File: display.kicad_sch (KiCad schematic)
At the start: 17 parts, among them Q1 ZXM61N03F, U1 E2206KS0E1

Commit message: .
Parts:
- added A1: Arduino_Nano_Every, Module:Arduino_Nano, symbol rsx_Modules:Arduino_Nano_Every
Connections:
- net GND: now also A1.29 (GND), A1.4 (GND)
- net Connect to power switch: now reaches C10.1, C9.1, SRP3012TA-100M1.1, U1.15, U1.16
- net A2: now reaches U1.10
- net A3: now reaches U1.11
- net D2: now reaches U1.12
- net SCL: now reaches U1.13
- net SDA: now reaches U1.14
- net A0: now reaches U1.8
- net A1: now reaches U1.9
- new net 10: A1.21 (A2)
- new net 11: A1.22 (A3)
- new net 12: A1.5 (D2)
- new net 13: A1.24 (SCL/A5)
- new net 14: A1.23 (SDA/A4)
- new net 8: A1.19 (A0)
- new net 9: A1.20 (A1)

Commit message: Nano every
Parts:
- removed Q1: ZXM61N03F, Package_TO_SOT_SMD:SOT-23, symbol Transistor_FET:ZXM61N03F
- removed U1: E2206KS0E1, SOIC_096NL_PUL, symbol rsx_misc:Graphic Display
- added J3: FH34SRJ-24S-0.5SH_99_, rsx_headers_communications:HRS_FH34SRJ-24S-0.5SH_99_, symbol rsx_Header_communication:FH34SRJ-24S-0.5SH_99_
- added Q1, Q2: ZXM61N03F, rsx_packages_TO_SOT:SOT-23, symbol rsx_Transistors:ZXM61N03F
- added SW3: Button-THT - 2-1825910-7, rsx_HID:2-1825910-7, symbol rsx_HID:Button-THT - 2-1825910-7
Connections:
- net 12: now also A1.15 (MISO)
- net A0: now also J3.8
- net A1: now also J3.9
- net A2: now also J3.10
- net A3: now also J3.11
- net GND: now also J3.17
- net SCL: now also J3.13
- net SDA: now also J3.14
- net at C2.2: now also J3.18
- net at C6.2, CR3.1: now also J3.21
- net at R1.2: now also J3.3, Q1.2 (S)
- net at C7.2, CR1.2: now also J3.23
- net at C3.2: now also J3.20
- net at C4.2: now also J3.22
- net at C5.2: now also J3.24
- net at C1.2: now also J3.5
- net at A1.10 (D7): now also Q2.1 (G)
- net Display Power: now reaches A1.17 (3V3)
- net Display Power: now also Q2.3 (D)
- net at A1.30 (VIN): now also SW3.1
- net at C8.1, CR3.2, SRP3012TA-100M1.2: now also Q1.3 (D)
- net Connect to power switch: no longer names the net of C10.1, C9.1, SRP3012TA-100M1.1
- net Connect to power switch: now also J3.15, J3.16, Q2.2 (S)
- new net: J3.2, Q1.1 (G)
- new net +3.3V: SW3.2
- new net MISO: J3.12
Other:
- moved on the sheet: A1, C1, R1

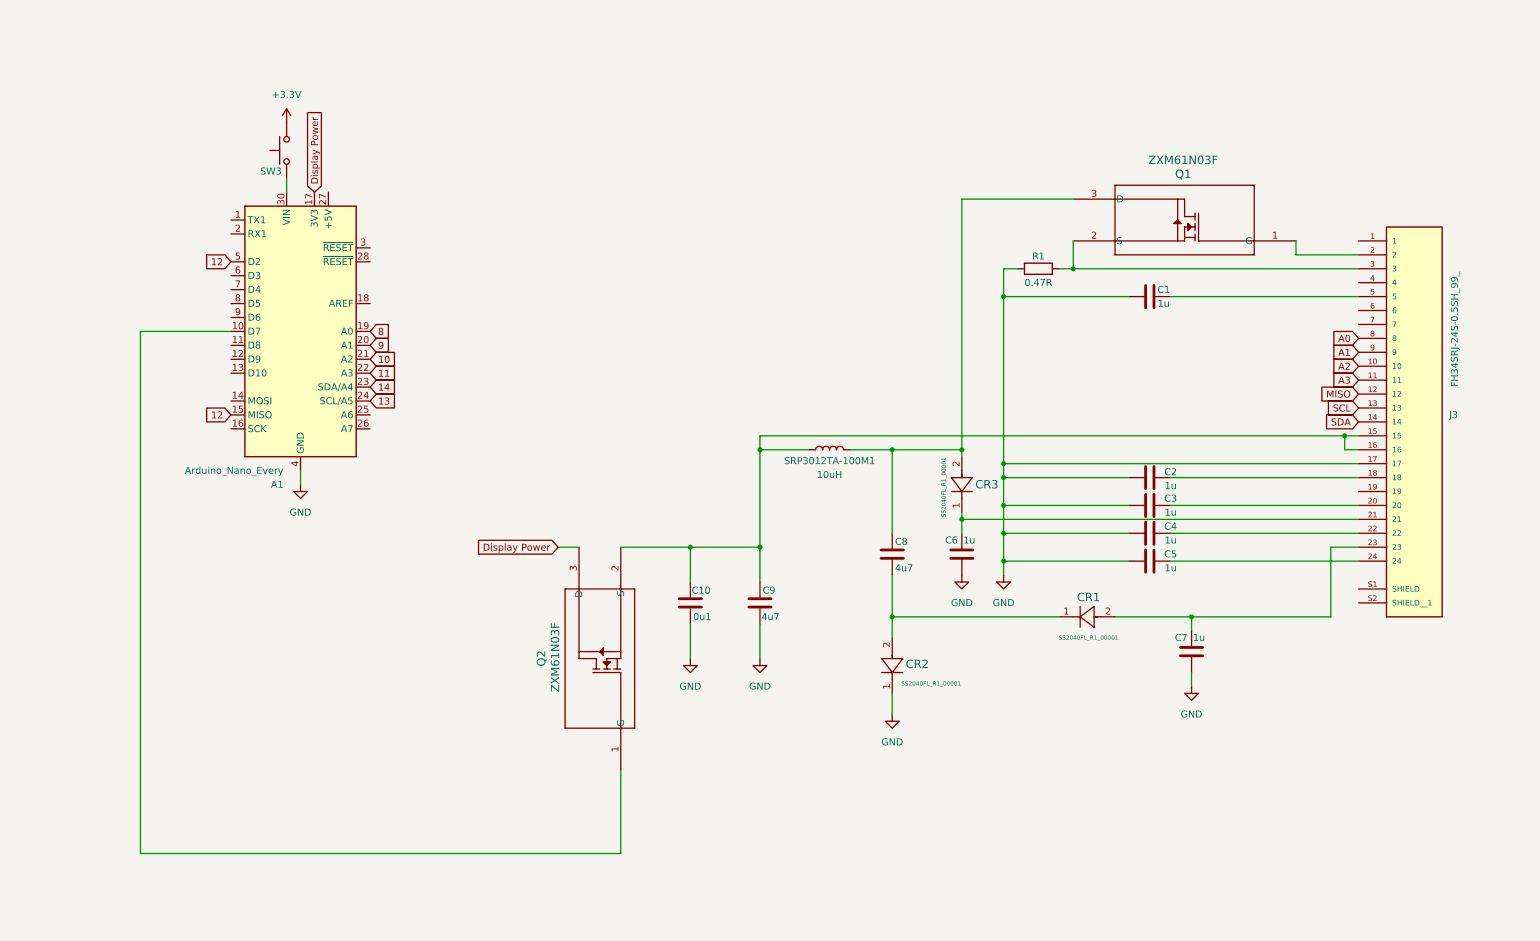
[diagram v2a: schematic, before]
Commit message: Schematic with Pico
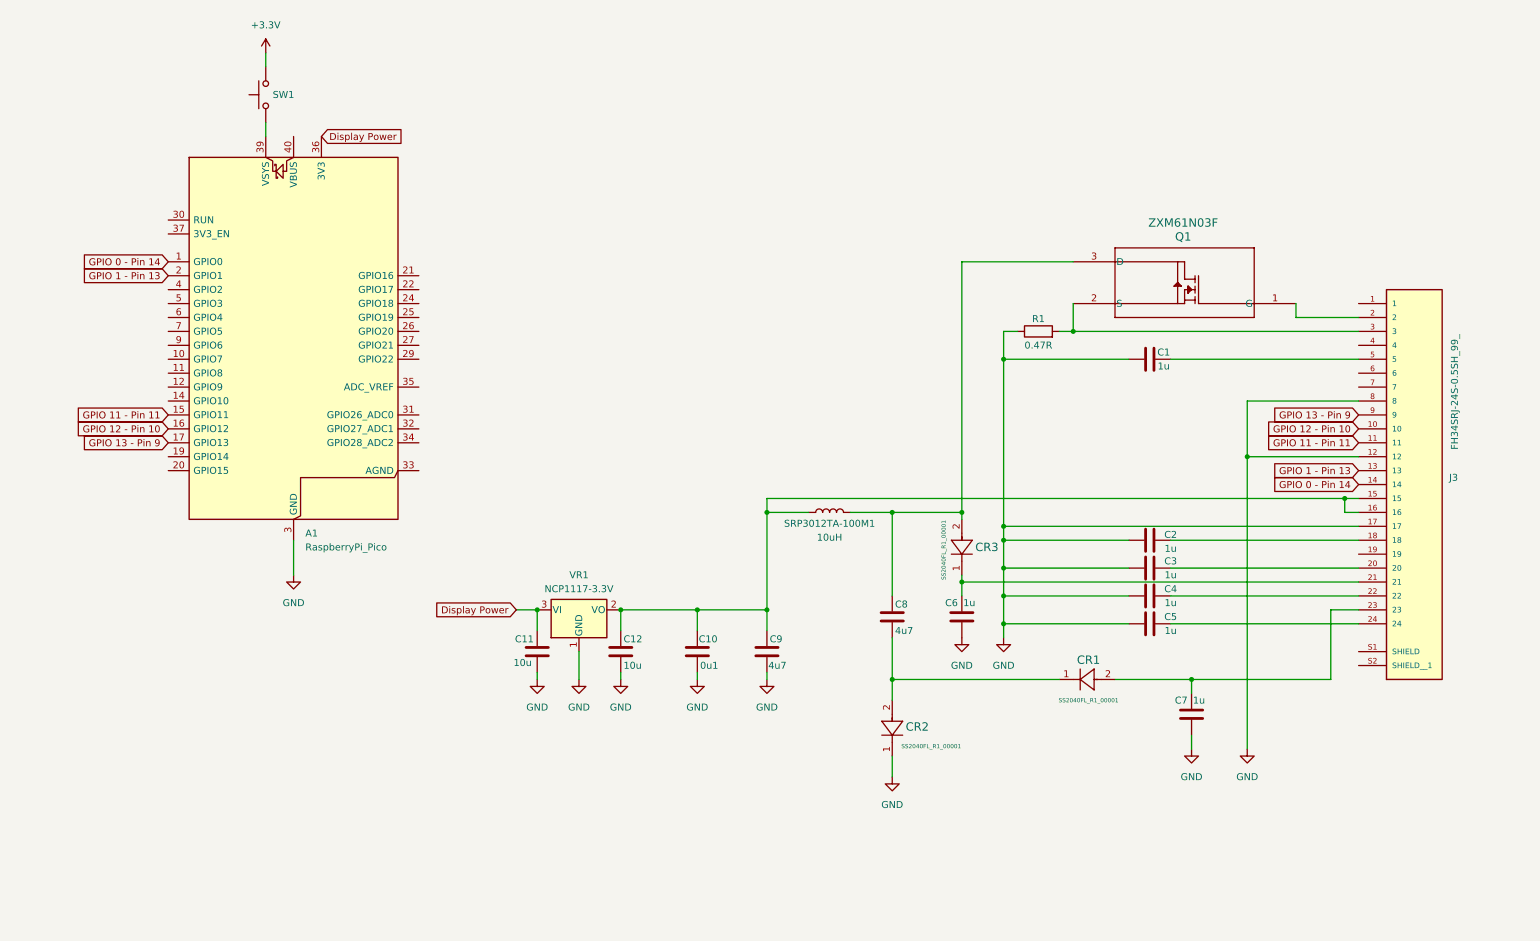
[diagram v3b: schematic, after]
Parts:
- removed A1: Arduino_Nano_Every, Module:Arduino_Nano, symbol rsx_Modules:Arduino_Nano_Every
- removed Q2: ZXM61N03F, rsx_packages_TO_SOT:SOT-23, symbol rsx_Transistors:ZXM61N03F
- removed SW3: Button-THT - 2-1825910-7, rsx_HID:2-1825910-7, symbol rsx_HID:Button-THT - 2-1825910-7
- added A1: RaspberryPi_Pico, Module:RaspberryPi_Pico_Common_Unspecified, symbol MCU_Module:RaspberryPi_Pico
- added C11, C12: 10u, rsx_capacitors:C_0805_2012Metric, symbol rsx_Capacitors:10u
- added SW1: Button-THT - 2-1825910-7, rsx_HID:2-1825910-7, symbol rsx_HID:Button-THT - 2-1825910-7
- added VR1: NCP1117-3.3V, rsx_packages_TO_SOT:SOT-223-3_TabPin2, symbol rsx_voltage_regulation:NCP1117-3.3V
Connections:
- net A0 is gone; now on net GND: J3.8
- net MISO is gone; now on net GND: J3.12
- net +3.3V: now also SW1.2
- net Display Power: now also A1.36 (3V3), C11.1, VR1.3 (VI)
- net GND: now also A1.13 (GND), A1.18 (GND), A1.23 (GND), A1.28 (GND), A1.3 (GND), A1.38 (GND), A1.8 (GND), C11.2, C12.2, VR1.1 (GND)
- net at C10.1, C9.1, J3.15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: now also C12.1, VR1.2 (VO)
- net A1 renamed GPIO 13 - Pin 9
- net GPIO 13 - Pin 9: now also A1.17 (GPIO13)
- net A2 renamed GPIO 12 - Pin 10
- net GPIO 12 - Pin 10: now also A1.16 (GPIO12)
- net A3 renamed GPIO 11 - Pin 11
- net GPIO 11 - Pin 11: now also A1.15 (GPIO11)
- net SCL renamed GPIO 1 - Pin 13
- net GPIO 1 - Pin 13: now also A1.2 (GPIO1)
- net SDA renamed GPIO 0 - Pin 14
- net GPIO 0 - Pin 14: now also A1.1 (GPIO0)
- new net: A1.39 (VSYS), SW1.1
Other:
- moved on the sheet: C1, C10, C2, C3, C4, C5, C6, C7, C8, C9, CR1, CR2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

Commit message: Pico connected to display (mostly???)
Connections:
- net +3.3V: now also SW1.1; no longer SW1.2
- net GND: no longer J3.12
- net at A1.39 (VSYS): now also SW1.2; no longer SW1.1
- net GP17 - Pin 12 CSB: now reaches A1.22 (GPIO17)
- net GP17 - Pin 12 CSB: now also J3.12
- net GP18 - Pin 13 SCL: now reaches A1.24 (GPIO18)
- net GP18 - Pin 13 SCL: now also J3.13
- net GP19 - Pin 14 SDA: now reaches A1.25 (GPIO19)
- net GP19 - Pin 14 SDA: now also J3.14
- net GPIO 0 - Pin 14: no longer names the net of A1.1 (GPIO0)
- net GPIO 0 - Pin 14: no longer J3.14
- net GPIO 1 - Pin 13: no longer names the net of A1.2 (GPIO1)
- net GPIO 1 - Pin 13: no longer J3.13
- net GPIO 11 - Pin 11 renamed GP11 - Pin 10 RST
- net GP11 - Pin 10 RST: no longer J3.11
- net GPIO 12 - Pin 10 renamed GP12 - Pin 10
- net GP12 - Pin 10: no longer A1.16 (GPIO12)
- net GPIO 13 - Pin 9 renamed GP13 - Pin 9
- net GP13 - Pin 9: no longer A1.17 (GPIO13)
- new net GP11 - Pin 11: J3.11
- new net GP12 - Pin 11 DC: A1.16 (GPIO12)
- new net GP13 - Pin 9 Busy: A1.17 (GPIO13)
- no-connect marks 0 -> 32
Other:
- moved on the sheet: A1, CR2, SW1

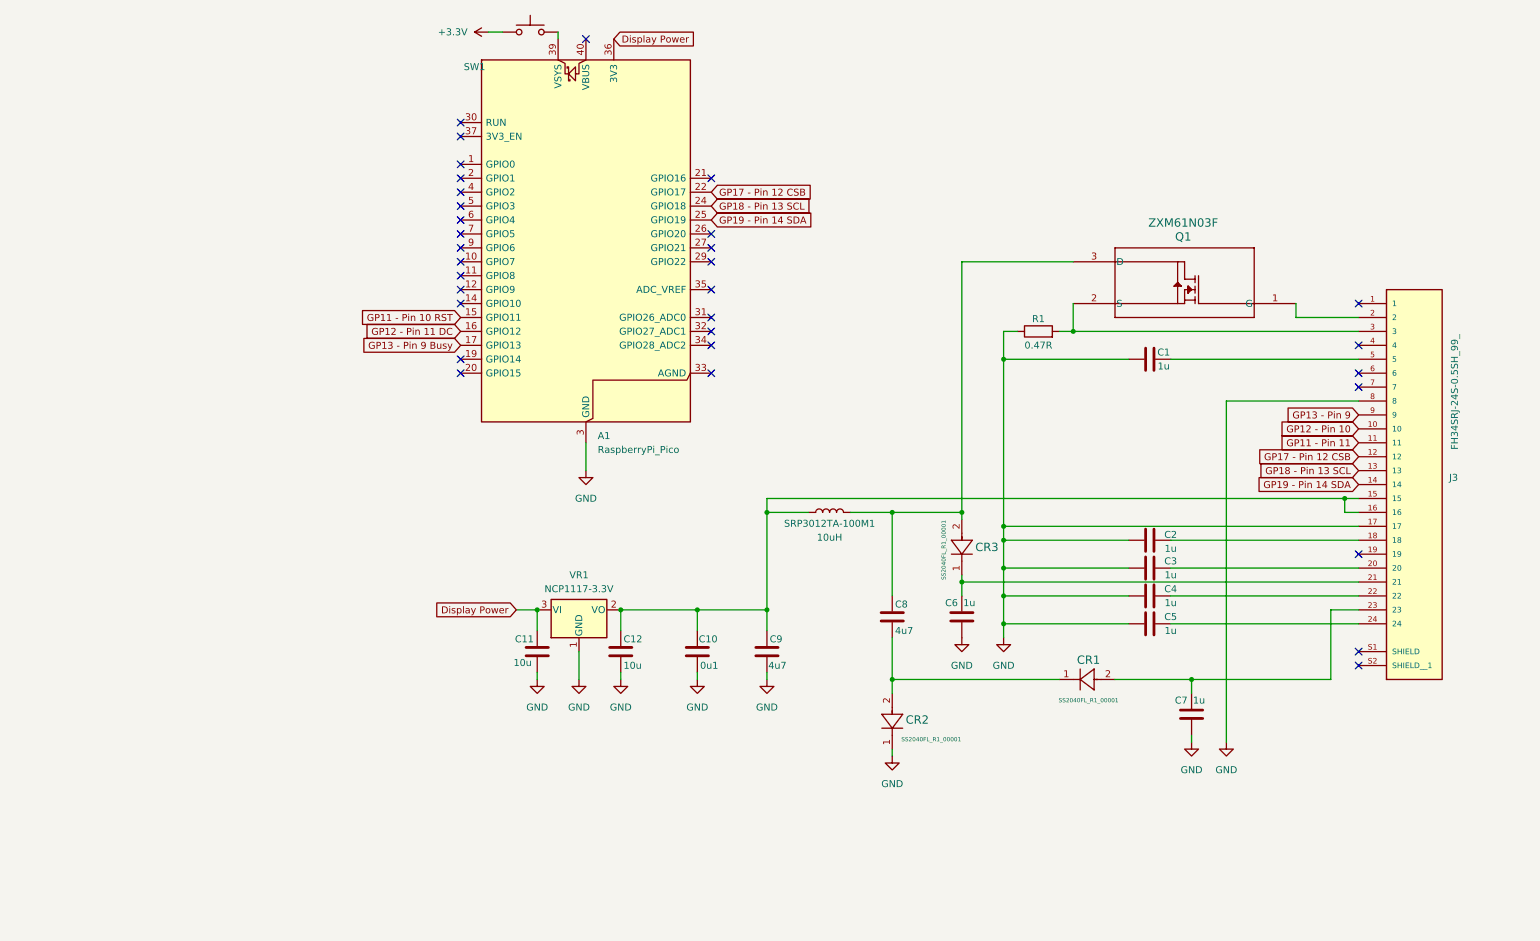
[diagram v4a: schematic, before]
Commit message: Display + Pico + voltage regulator
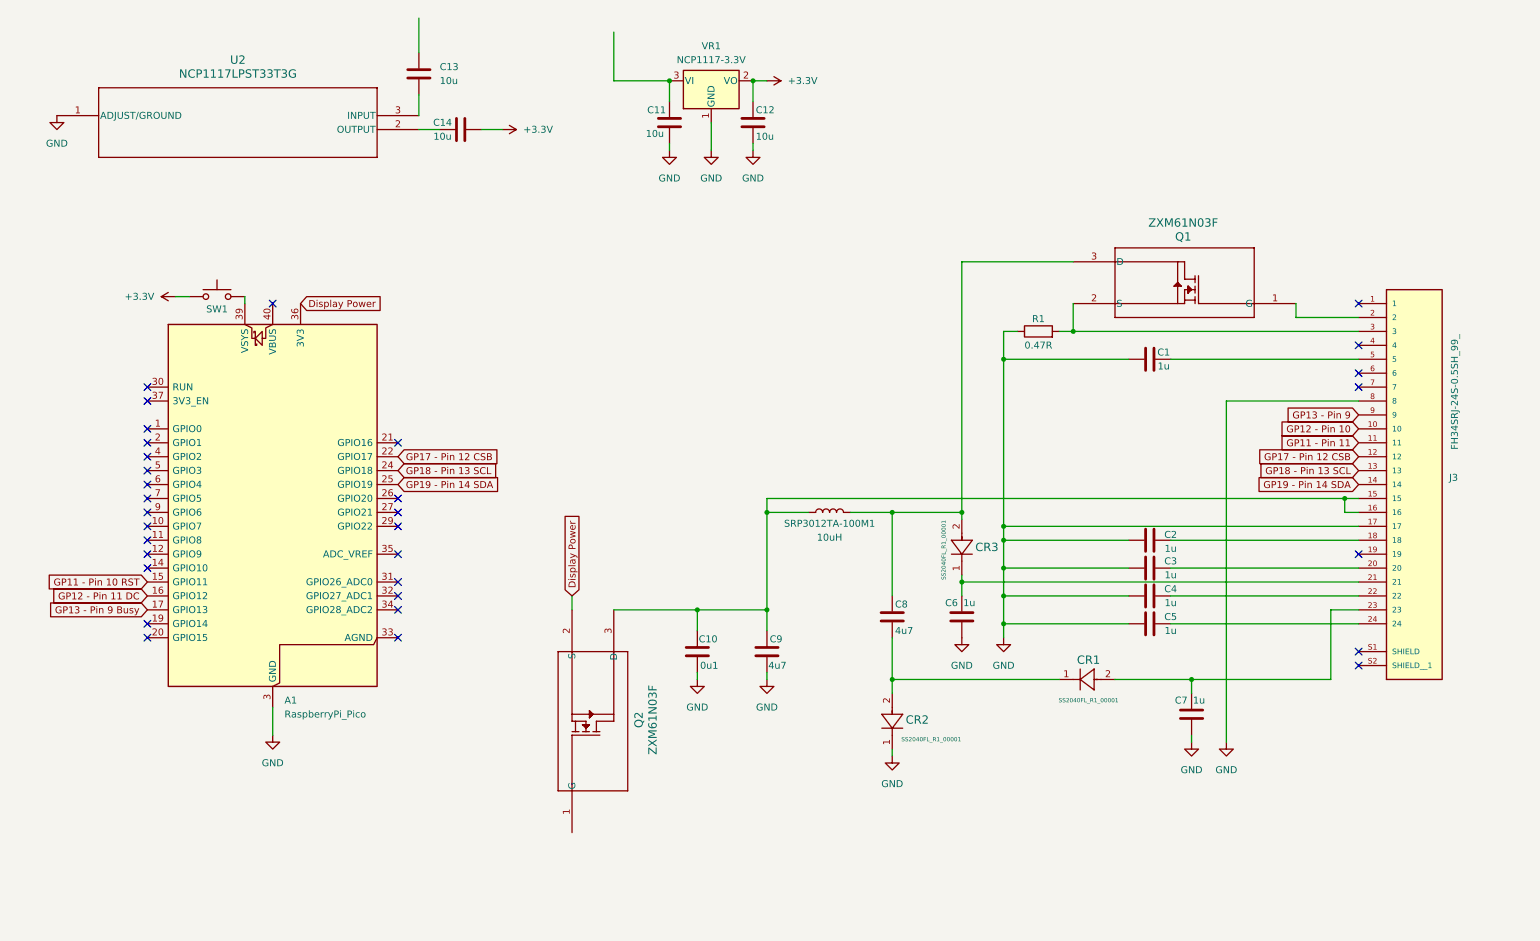
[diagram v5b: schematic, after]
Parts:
- added C13, C14: 10u, rsx_capacitors:C_0805_2012Metric, symbol rsx_Capacitors:10u
- added Q2: ZXM61N03F, rsx_packages_TO_SOT:SOT-23, symbol rsx_Transistors:ZXM61N03F
- added U2: NCP1117LPST33T3G, SOT223-3_ONS, symbol NCP1117:NCP1117LPST33T3G
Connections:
- net +3.3V: now also C12.1, VR1.2 (VO), C14.2
- net Display Power: now also Q2.2 (S); no longer C11.1, VR1.3 (VI)
- net GND: now also U2.1 (ADJUST/GROUND)
- net at C10.1, C9.1, J3.15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: now also Q2.3 (D); no longer C12.1, VR1.2 (VO)
- new net: C14.1, U2.2 (OUTPUT)
- new net: C13.2, U2.3 (INPUT)
- new net: C11.1, VR1.3 (VI)
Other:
- moved on the sheet: A1, C11, C12, SW1, VR1

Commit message: new
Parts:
- added C15: C, symbol Device:C
- added R2: R, symbol Device:R
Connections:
- net GND: now also C15.2
- net at SW1.2: now also A1.40 (VBUS); no longer A1.39 (VSYS)
- net at C10.1, C9.1, J3.15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: now also Q2.2 (S); no longer Q2.3 (D)
- net at Q2.1 (G): now also C15.1, R2.2
- net Display Power: no longer names the net of A1.36 (3V3)
- net Display Power: no longer Q2.2 (S)
- new net display power: Q2.3 (D)
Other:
- moved on the sheet: CR2, SW1

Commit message: Update display.kicad_sch
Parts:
- removed C12, C13, C14: 10u, rsx_capacitors:C_0805_2012Metric, symbol rsx_Capacitors:10u
- removed C15: C, symbol Device:C
- removed R2: R, symbol Device:R
- removed U2: NCP1117LPST33T3G, SOT223-3_ONS, symbol NCP1117:NCP1117LPST33T3G
- removed VR1: NCP1117-3.3V, rsx_packages_TO_SOT:SOT-223-3_TabPin2, symbol rsx_voltage_regulation:NCP1117-3.3V
- added C16, C18: 10u, rsx_capacitors:C_0805_2012Metric, symbol rsx_Capacitors:10u
- added R2: 100K, rsx_resistors:R_0603_1608Metric, symbol rsx_Resistors:100K
- added R4: 330R, rsx_resistors:R_0603_1608Metric, symbol rsx_Resistors:330R
- added U1: NCP1117LPST33T3G, SOT223-3_ONS, symbol NCP1117:NCP1117LPST33T3G
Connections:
- net display power is gone; now on net +3.3V: Q2.3 (D)
- net +3.3V: now also C16.1, U1.2 (OUTPUT)
- net GND: now also C16.2, C18.2, R2.2, U1.1 (ADJUST/GROUND)
- net at Q2.1 (G): now also C11.1, R2.1, R4.2
- net GP2 - Pin 13 SCLK: now reaches A1.4 (GPIO2)
- net GP2 - Pin 13 SCLK: now also J3.13
- net GP3 - Pin 14 SDA: now reaches A1.5 (GPIO3)
- net GP3 - Pin 14 SDA: now also J3.14
- net GP6 - Display_EN: now reaches A1.6 (GPIO4)
- net GP6 - Display_EN: now also R4.1
- net GP18 - Pin 13 SCL: no longer names the net of A1.24 (GPIO18)
- net GP18 - Pin 13 SCL: no longer J3.13
- net GP19 - Pin 14 SDA: no longer names the net of A1.25 (GPIO19)
- net GP19 - Pin 14 SDA: no longer J3.14
- new net: C18.1, U1.3 (INPUT)

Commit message: 11/08/25
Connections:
- net GP13 - Pin 9 is gone; now on net GP13 - Pin 9 Busy: J3.9
- net GP11 - Pin 11 renamed GP11 - Pin 11 DC
- net GP12 - Pin 10 renamed GP12 - Pin 10 RST
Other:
- moved on the sheet: A1, C11, Q2, R2, R4, SW1
